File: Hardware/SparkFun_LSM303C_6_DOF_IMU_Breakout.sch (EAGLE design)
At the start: 24 parts, among them U1 LSM303C, U2 LM3880

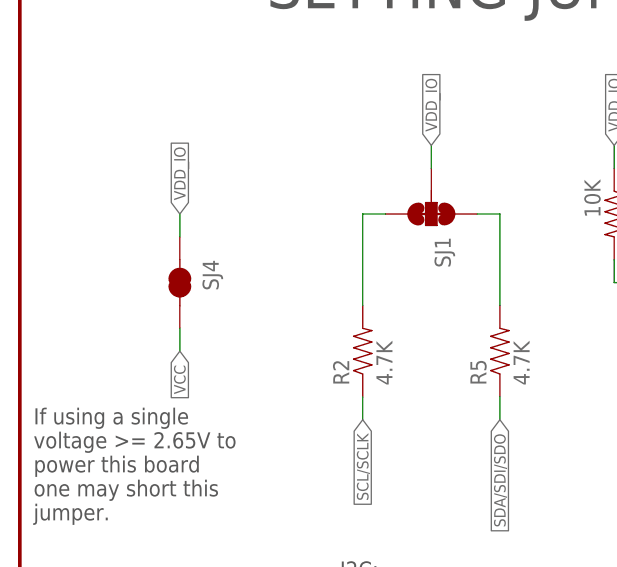
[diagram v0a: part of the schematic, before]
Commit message: Renamed SJ4 & moved a dim to layer 47
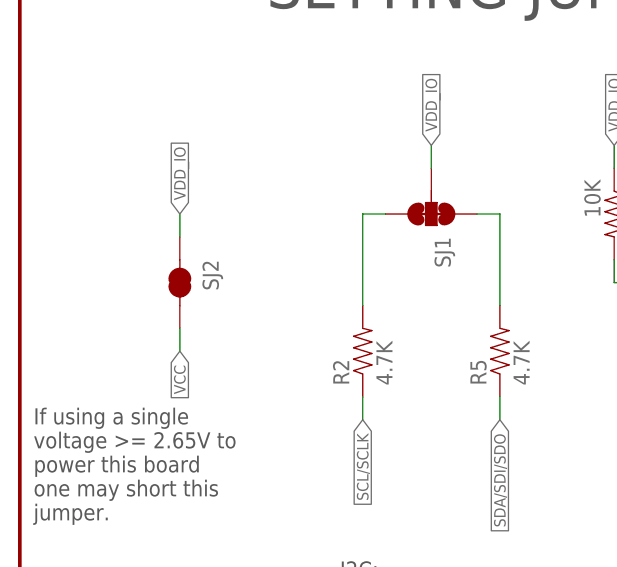
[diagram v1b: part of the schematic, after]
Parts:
- renumbered SJ4 to SJ2
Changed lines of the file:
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@@
 <?xml version="1.0" encoding="utf-8"?>
 <!DOCTYPE eagle SYSTEM "eagle.dtd">
-<eagle version="7.2.0">
+<eagle version="7.3.2">
 <drawing>
 <settings>
@@
 <part name="SUPPLY2" library="SparkFun-Aesthetics" deviceset="VCC" device=""/>
 <part name="SJ1" library="SparkFun-Passives" deviceset="JUMPER-PAD-3-NC_BY_TRACE" device=""/>
-<part name="SJ4" library="SparkFun-Passives" deviceset="JUMPER-PAD-2-NC_BY_TRACE" device=""/>
+<part name="SJ2" library="SparkFun-Passives" deviceset="JUMPER-PAD-2-NC_BY_TRACE" device=""/>
 <part name="TP1" library="SparkFun-Passives" deviceset="TEST-POINT" device="TP_15TH_THRU" value="VDD_TP"/>
 <part name="STANDOFF1" library="SparkFun-Electromechanical" deviceset="STAND-OFF" device=""/>
@@
 <attribute name="NAME" x="46.101" y="71.12" size="1.778" layer="95" rot="R270"/>
 </instance>
-<instance part="SJ4" gate="G$1" x="17.78" y="66.04" smashed="yes" rot="R270">
+<instance part="SJ2" gate="G$1" x="17.78" y="66.04" smashed="yes" rot="R270">
 <attribute name="NAME" x="20.32" y="68.58" size="1.778" layer="95" rot="R270"/>
 </instance>
@@
 <segment>
 <wire x1="17.78" y1="58.42" x2="17.78" y2="60.96" width="0.1524" layer="91"/>
-<pinref part="SJ4" gate="G$1" pin="2"/>
+<pinref part="SJ2" gate="G$1" pin="2"/>
 <label x="17.78" y="58.42" size="1.27" layer="95" rot="R270" xref="yes"/>
 </segment>
@@
 <segment>
 <wire x1="17.78" y1="71.12" x2="17.78" y2="73.66" width="0.1524" layer="91"/>
-<pinref part="SJ4" gate="G$1" pin="1"/>
+<pinref part="SJ2" gate="G$1" pin="1"/>
 <label x="17.78" y="73.66" size="1.27" layer="95" rot="R90" xref="yes"/>
 </segment>

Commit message: Fixed typo in note
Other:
- note added: "Cut this jumper if using a Vdd_IO less than Vdd."
- note added: "I2C: XL slave address: 0x1D MAG slave address: 0x1E"
- note added: "JUMPERS & PULL-UPS"
- note added: "Jumpers are connected by default and used by both I2C and SPI. They may be cut to tune an I2C bus when multiple devices are being used."
- note removed: "I2C: XL slave address: 0x1D MAG slage address: 0x1E"
- note removed: "If using a single voltage >= 2.65V to power this board one may short this jumper."
- note removed: "Jumpers are defaulted to I2C configuration. Cut them to use SPI"
- note removed: "SETTING JUMPERS"
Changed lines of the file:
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@@
 <?xml version="1.0" encoding="utf-8"?>
 <!DOCTYPE eagle SYSTEM "eagle.dtd">
-<eagle version="7.3.2">
+<eagle version="7.4.0">
 <drawing>
 <settings>
@@
 <text x="35.56" y="27.94" size="1.778" layer="97" font="vector">I2C:
   XL slave address:  0x1D
-  MAG slage address: 0x1E</text>
-<text x="55.88" y="99.06" size="5.08" layer="97" font="vector" align="center">SETTING JUMPERS</text>
+  MAG slave address: 0x1E</text>
+<text x="55.88" y="99.06" size="5.08" layer="97" font="vector" align="center">JUMPERS &amp; PULL-UPS</text>
 <text x="144.78" y="99.06" size="5.08" layer="97" font="vector" align="center">HEADERS</text>
 <text x="218.44" y="99.06" size="5.08" layer="97" font="vector" align="center">BYPASS</text>
@@
 <text x="171.45" y="13.97" size="3.81" layer="94" font="vector" align="top-left">&gt;DESIGNER</text>
 <text x="236.22" y="6.858" size="3.81" layer="94" font="vector">&gt;VERSION</text>
-<text x="1.524" y="52.07" size="1.778" layer="97" font="vector" align="top-left">If using a single
-voltage &gt;= 2.65V to
-power this board
-one may short this
-jumper.
-</text>
-<text x="35.56" y="20.32" size="1.778" layer="97" font="vector">Jumpers are defaulted to I2C
-configuration.  Cut them to use SPI</text>
+<text x="1.524" y="52.07" size="1.778" layer="97" font="vector" align="top-left">Cut this jumper if
+using a Vdd_IO less
+than Vdd.</text>
+<text x="35.56" y="25.4" size="1.778" layer="97" font="vector" align="top-left">Jumpers are connected by
+default and used by both I2C
+and SPI.  They may be cut to
+tune an I2C bus when multiple
+devices are being used.</text>
 <text x="134.62" y="157.48" size="1.9304" layer="97">VCC = 2.65V to 4.3V</text>
 </plain>
